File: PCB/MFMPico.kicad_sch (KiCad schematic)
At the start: 39 parts, among them J1 ECON34, J2 Conn_02x04_Odd_Even, J3 Micro_SD_Card, J4 Conn_01x16, J5 Conn_01x04, J6 Conn_01x02, J7 Conn_01x02, J8 Conn_01x02, J9 Conn_01x04, P1 CON20, Q1 BC547, SW1 SW_Push, U2 74LS03, U3 74LS03, U4 74LS03, U5 SN65HVD33DR, U6 74LS03

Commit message: Step not a pio program anymore, validated with mfm emulator.
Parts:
- removed Q1: BC547, Package_TO_SOT_THT:TO-92_Inline, symbol Transistor_BJT:BC547
- removed R12: 5.1K, Resistor_THT:R_Axial_DIN0207_L6.3mm_D2.5mm_P10.16mm_Horizontal, symbol Device:R
- J7: value Conn_01x02 -> DNP
- J8: value Conn_01x02 -> PLACE
- R4: value 100R -> DNP
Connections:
- net DRIVE_SEL: now also A1.29 (GPIO22), U6.8
- net ~DRIVE_SEL: now also U6.10, U6.9
- no-connect marks 27 -> 26
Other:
- note added: "5V but the RP2040 is 5V ish compatible."
- note added: "Desired behaviour: 1: DRIVE_SEL low, Write_gate low, DE low, RE high 2: DRIVE_SEL low, Write_gate high, DE low, RE high 2: DRIVE_SEL high, Write_gate low, DE high, RE high 3: DRIVE_SEL high, Write_gate high, DE low, RE low currently not as desired, but works enough"
- note added: "RE"
- moved on the sheet: C1, J3, U6C

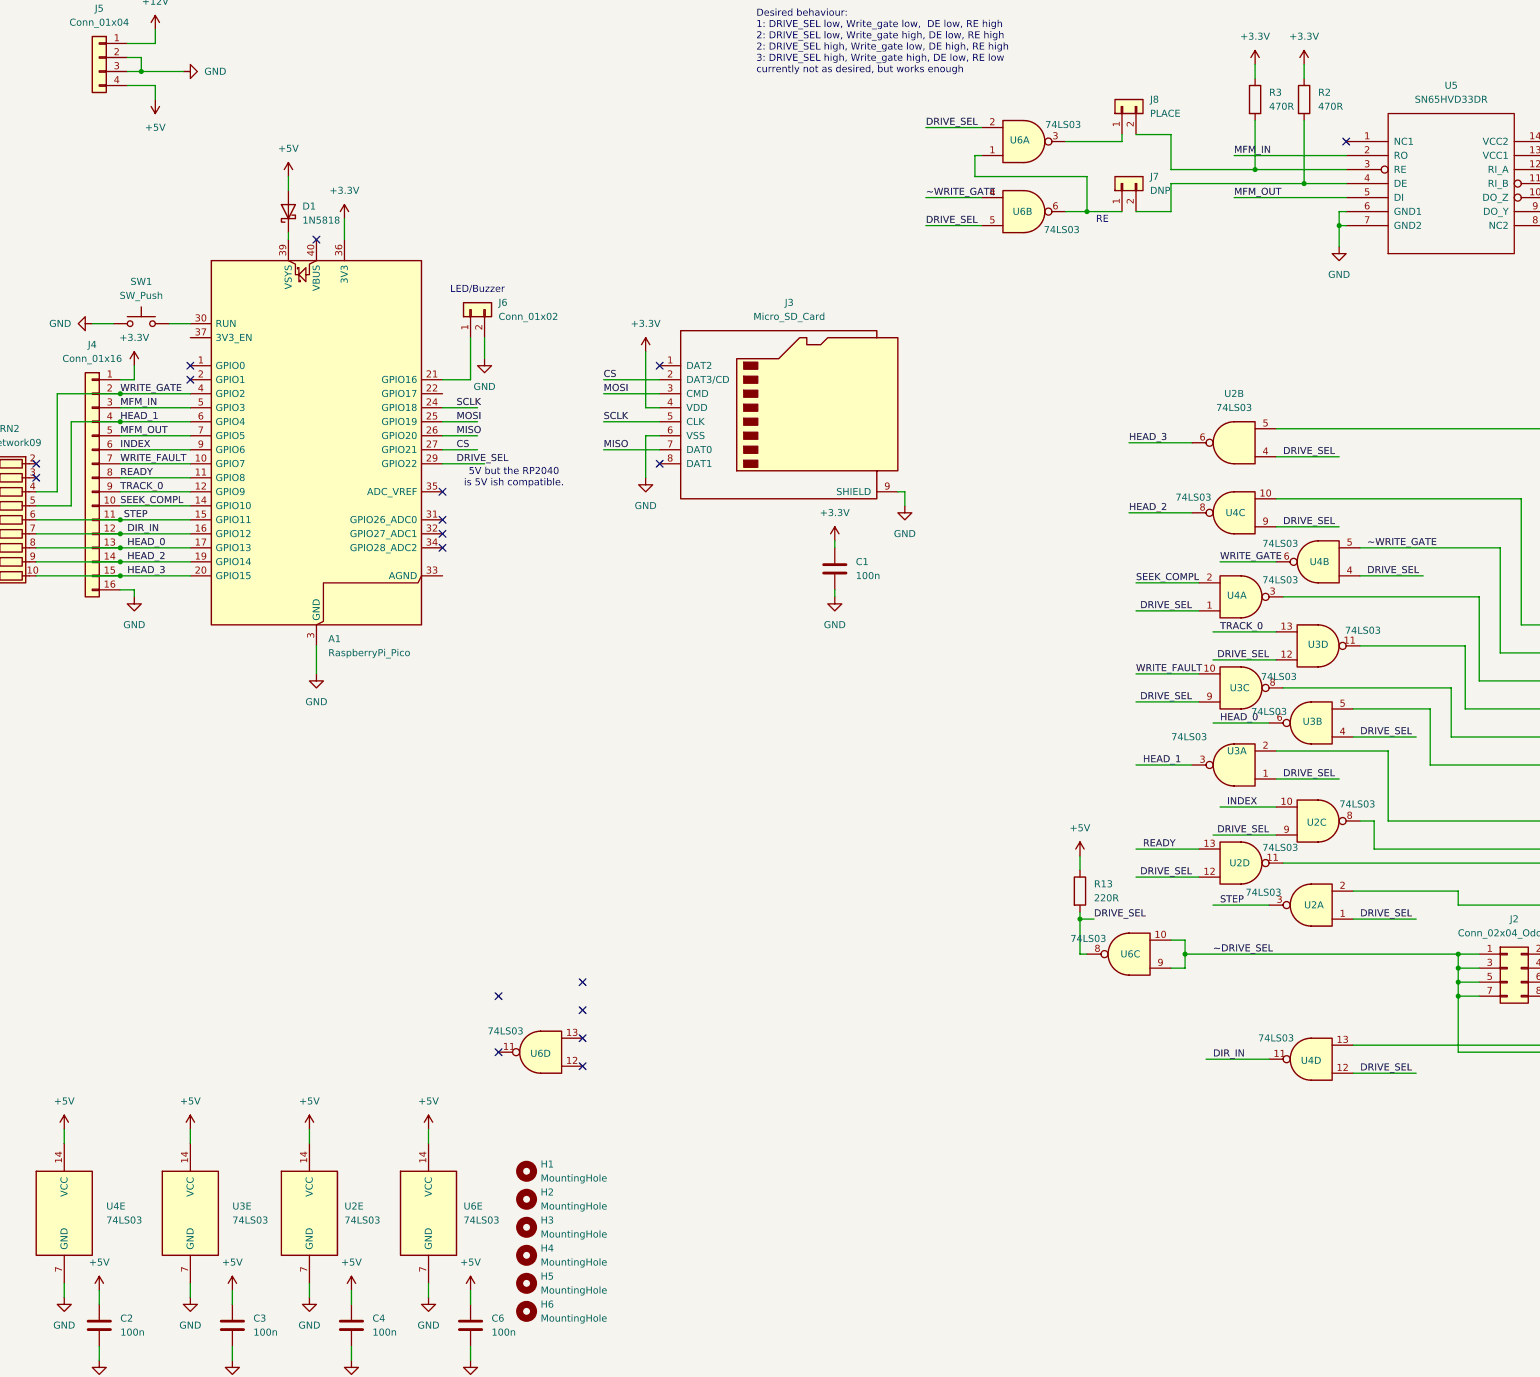
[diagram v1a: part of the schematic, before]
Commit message: moving to nor gates for drive sel slowly
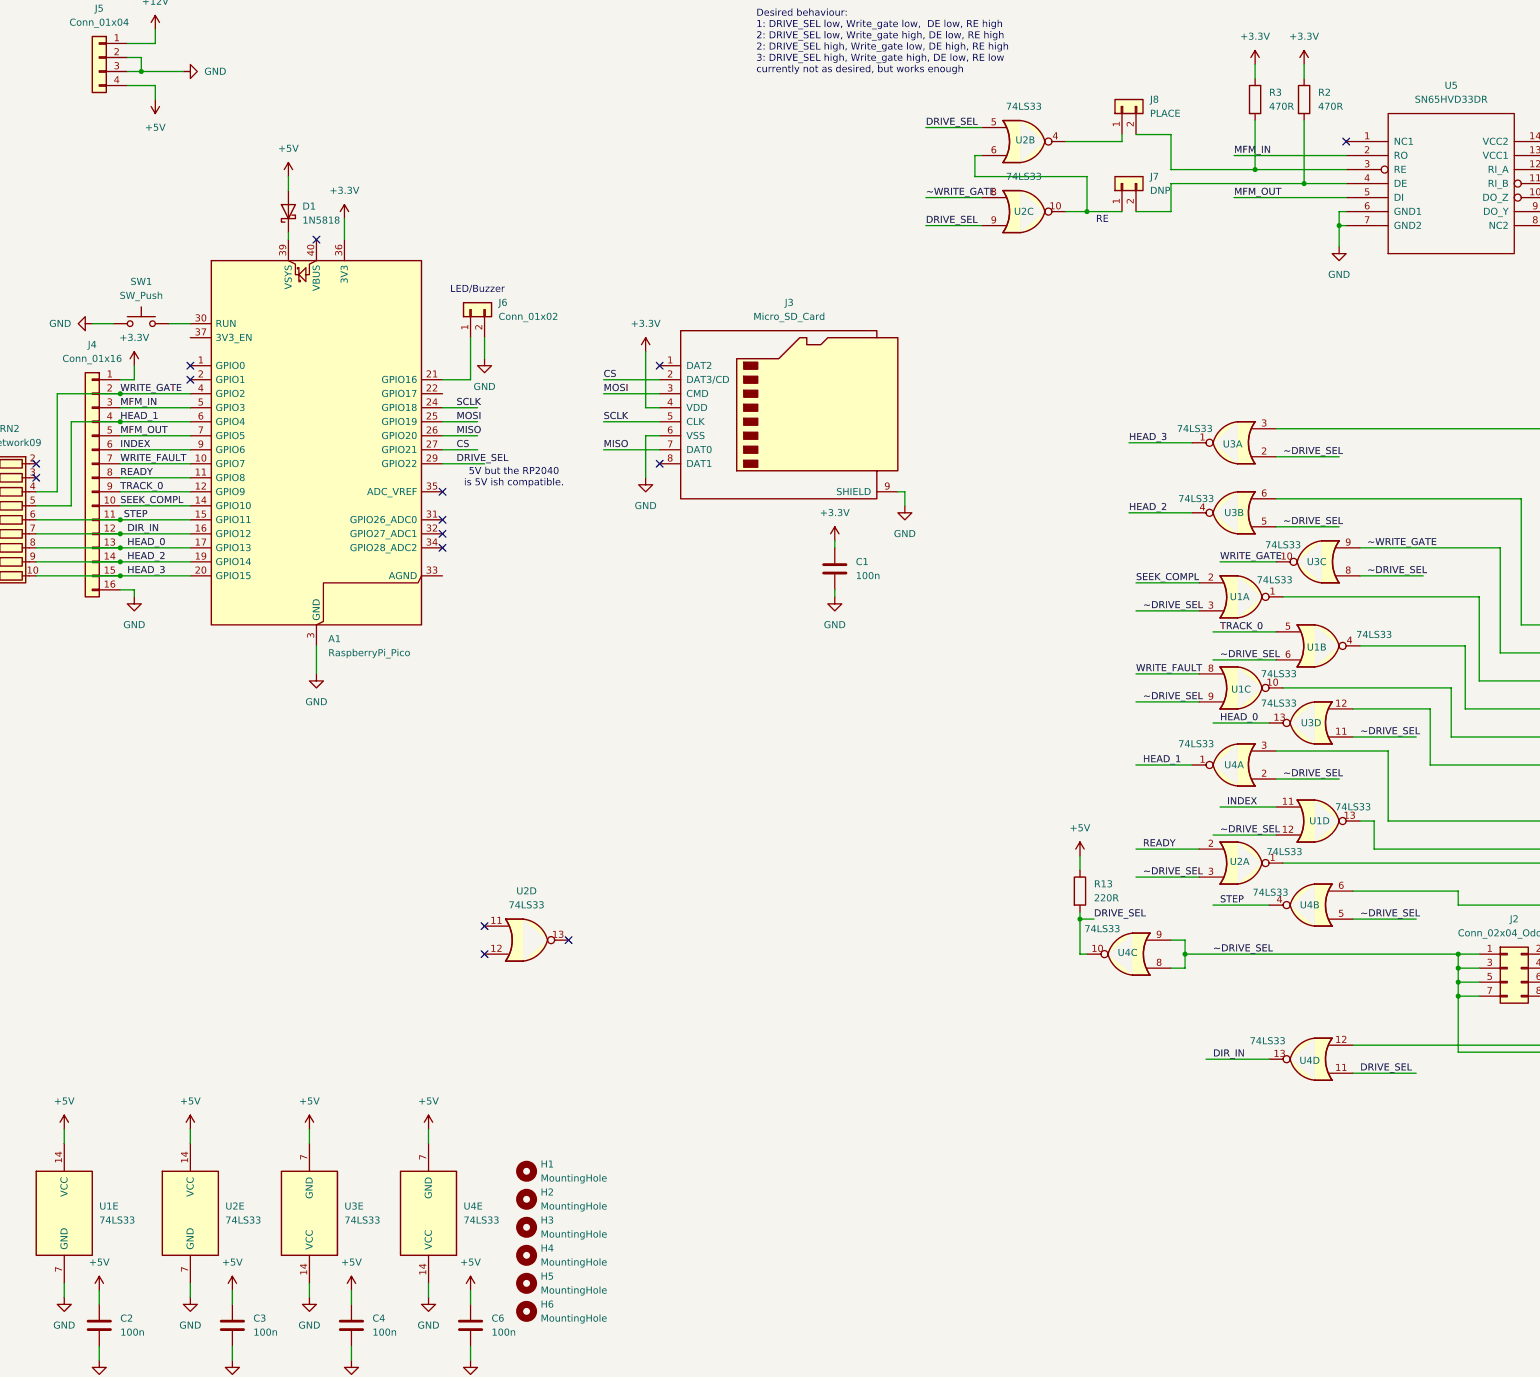
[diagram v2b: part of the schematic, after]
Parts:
- removed U2, U3, U4, U6: 74LS03, Package_DIP:DIP-14_W7.62mm, symbol 74xx:74LS03
- added U1, U2, U3, U4: 74LS33, symbol 74xx:74LS33
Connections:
- net +5V: now also U1.14 (VCC), U2.14 (VCC), U3.7 (GND), U4.7 (GND)
- net DIR_IN: now also U4.13
- net DRIVE_SEL: now also U2.5, U2.9, U4.10, U4.11
- net GND: now also U1.7 (GND), U2.7 (GND), U3.14 (VCC), U4.14 (VCC)
- net HEAD_0: now also U3.13
- net HEAD_1: now also U4.1
- net HEAD_2: now also U3.4
- net HEAD_3: now also U3.1
- net INDEX: now also U1.11
- net READY: now also U2.2
- net SEEK_COMPL: now also U1.2
- net STEP: now also U4.4
- net TRACK_0: now also U1.5
- net WRITE_FAULT: now also U1.8
- net WRITE_GATE: now also U3.10
- net ~DRIVE_SEL: now also U1.12, U1.3, U1.6, U1.9, U2.3, U3.11, U3.2, U3.5, U3.8, U4.2, U4.5, U4.8, U4.9
- net ~WRITE_GATE: now also U2.8, U3.9
- net at J7.1 (Pin_1): now also U2.10, U2.6
- net at J8.1 (Pin_1): now also U2.4
- net at J1.12 (Write_Fault): now also U1.10
- net at J1.4 (Head_2), RN1.4 (R3): now also U3.6
- net at J1.24 (Step), RN1.8 (R7): now also U4.6
- net at J1.8 (Seek_Complete): now also U1.1
- net at J1.34 (Direction_In), RN1.10 (R9): now also U4.12
- net at J1.10 (Track_0): now also U1.4
- net at J1.14 (Head_0), RN1.6 (R5): now also U3.12
- net at J1.18 (Head_1), RN1.7 (R6): now also U4.3
- net at J1.2 (Head_3/REDWR), RN1.3 (R2): now also U3.3
- net at J1.20 (Index): now also U1.13
- net at J1.22 (Ready): now also U2.1
- no-connect marks 26 -> 23

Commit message: wip on  nor gate version
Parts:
- removed C3: 100n, Capacitor_THT:C_Disc_D3.4mm_W2.1mm_P2.50mm, symbol Device:C
- removed J3: Micro_SD_Card, rik:microSD Hanbo Electronic TF-018, symbol Connector:Micro_SD_Card
- removed R13: 220R, Resistor_THT:R_Axial_DIN0207_L6.3mm_D2.5mm_P10.16mm_Horizontal, symbol Device:R
- removed RN2: R_Network09, Resistor_THT:R_Array_SIP10, symbol Device:R_Network09
- removed U1, U2: 74LS33, symbol 74xx:74LS33
- removed unit 4 of U4
- added C7, C8, C9: 100n, Capacitor_SMD:C_0603_1608Metric_Pad1.08x0.95mm_HandSolder, symbol Device:C
- added J3: Micro_SD_Card_Det1, rik:microSD Hanbo Electronic TF-018, symbol Connector:Micro_SD_Card_Det1
- added JP1, JP2, JP3, JP4, JP5, JP6, JP7, JP8: SolderJumper_2_Open, Jumper:SolderJumper-2_P1.3mm_Open_Pad1.0x1.5mm, symbol Jumper:SolderJumper_2_Open
- added R10, R11, R5, R6, R7, R8, R9: 1K, Resistor_SMD:R_0603_1608Metric, symbol Device:R
- added U1: 74LVC1G02, Package_TO_SOT_SMD:SOT-23-5_HandSoldering, symbol 74xGxx:74LVC1G02
- added U6: 74LS05, Package_DIP:DIP-14_W7.62mm, symbol 74xx:74LS05
- added U7, U8: SN74LVC1G00DBV, Package_TO_SOT_SMD:SOT-23-5_HandSoldering, symbol 74xGxx:SN74LVC1G00DBV
- C1, C2, C4, C5, C6: footprint Capacitor_THT:C_Disc_D3.4mm_W2.1mm_P2.50mm -> Capacitor_SMD:C_0603_1608Metric_Pad1.08x0.95mm_HandSolder
- U3, U4: footprint (none) -> Package_DIP:DIP-14_W7.62mm
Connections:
- net +3.3V: now also C7.1, C8.1, C9.1, J3.4 (VDD), R10.1, R11.1, R5.1, R6.1, R7.1, R8.1, R9.1, U1.5 (VCC), U7.5 (VCC), U8.5 (VCC)
- net +5V: now also U3.14 (VCC), U4.14 (VCC), U6.14 (VCC); no longer U3.7 (GND), U4.7 (GND)
- net DIR_IN: now also U3.10, R8.2
- net GND: now also U3.7 (GND), U4.7 (GND), C7.2, C8.2, C9.2, J3.6 (VSS), J3.SH (SHIELD), U1.3 (GND), U6.7 (GND), U7.3 (GND), U8.3 (GND); no longer U3.14 (VCC), U4.14 (VCC)
- net HEAD_0: now also R9.2
- net HEAD_1: now also R6.2
- net HEAD_2: now also R10.2
- net HEAD_3: now also R11.2
- net INDEX: now also U6.9
- net MOSI: now also J3.3 (CMD), JP2.2 (B), JP3.2 (B); no longer A1.25 (GPIO19)
- net READY: now also U6.11
- net SCLK: now also A1.22 (GPIO17), J3.5 (CLK), JP1.2 (B); no longer A1.24 (GPIO18)
- net SEEK_COMPL: now also U6.1
- net STEP: now also R7.2
- net TRACK_0: now also U6.3
- net WRITE_FAULT: now also U6.5
- net WRITE_GATE: now also U4.10, R5.2; no longer U3.10
- net ~DRIVE_SEL: now also U1.2, U8.1, U8.2; no longer U4.9
- net ~WRITE_GATE: now also U4.9, U1.1, U7.2; no longer U3.9
- net at J1.22 (Ready): now also U6.10
- net at J1.8 (Seek_Complete): now also U6.2
- net at J7.1 (Pin_1): now also U1.4
- net at J1.10 (Track_0): now also U6.4
- net at J1.12 (Write_Fault): now also U6.6
- net at J1.20 (Index): now also U6.8
- net at J1.34 (Direction_In), RN1.10 (R9): now also U3.9
- net at J8.1 (Pin_1): now also U7.4
- net CS: no longer names the net of A1.27 (GPIO21)
- net CS: now also JP7.1 (A), JP8.1 (A)
- net DRIVE_SEL renamed CS/D3
- net CS/D3: now also J3.2 (DAT3/CD), JP7.2 (B); no longer U4.10
- net MISO: no longer names the net of A1.26 (GPIO20)
- net MISO: now also JP5.1 (A), JP6.1 (A)
- new net: A1.24 (GPIO18), JP1.1 (A), JP2.1 (A)
- new net: U7.1, U8.4
- new net: A1.25 (GPIO19), JP3.1 (A), JP4.1 (A)
- new net D1: J3.8 (DAT1), JP6.2 (B)
- new net D2: J3.1 (DAT2), JP8.2 (B)
- new net MISO/D0: J3.7 (DAT0), JP4.2 (B), JP5.2 (B)
- no-connect marks 23 -> 19
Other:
- note added: "Desired behaviour: 1: ~DRIVE_SEL high, ~Write_gate low, DE low, RE high 2: ~DRIVE_SEL high, ~Write_gate high, DE low, RE high 2: ~DRIVE_SEL low, ~Write_gate low, DE high, RE high 3: ~DRIVE_SEL low, ~Write_gate high, DE low, RE low currently not as desired, but works enough"
- note removed: "5V but the RP2040 is 5V ish compatible."
- note removed: "Desired behaviour: 1: DRIVE_SEL low, Write_gate low, DE low, RE high 2: DRIVE_SEL low, Write_gate high, DE low, RE high 2: DRIVE_SEL high, Write_gate low, DE high, RE high 3: DRIVE_SEL high, Write_gate high, DE low, RE low currently not as desired, but works enough"
- note removed: "RE"
- moved on the sheet: A1, C1, C2, D1, J4, J5, J6, SW1, U3C, U3E, U4C, U4E
